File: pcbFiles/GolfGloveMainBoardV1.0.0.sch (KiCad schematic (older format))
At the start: 79 parts, among them J1 USB_C_Receptacle, J10 A-1JB, J11 Conn_01x16_Male, J12 HOST_WAKE, J13 TP4, J14 Conn_01x02_Male, J15 Conn_01x02_Male, J2 BT_UART, J3 USB_C_Receptacle, J4 Conn_01x01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

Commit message: Update the circuit schematic
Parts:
- removed C1, C10, C11, C12, C15, C16, C17, C18, C19, C2, C20, C27, C3, C34, C4, C5, C6, C7: C, Capacitors_SMD:C_0402, symbol C
- removed D1: LED, LEDs:LED_0603, symbol LED
- removed J14, J15, J6, J7, J8, J9: Conn_01x02_Male, Pin_Headers:Pin_Header_Straight_1x02_Pitch2.54mm, symbol Conn_01x02_Male
- removed L1: L, Inductors_SMD:L_0805, symbol L
- removed R1, R10, R12, R13, R14, R2, R3, R5, R6, R7, R8, R9: R, Capacitors_SMD:C_0603, symbol R
- removed SW2: SW_Push, Buttons_Switches_SMD:SW_SPST_B3S-1000, symbol SW_Push
- removed U1, U2: LSM9DS1TR, LSM9DS1TR:PQFN43P300X350X102-24N, symbol LSM9DS1TR
- removed U3: TPS63001DRCT, TPS63001DRCT:SON50P300X300X100-11N, symbol TPS63001DRCT
- removed U5: MCP73831T-2ACI/OT, MCP73831T-2ACI_OT:SOT95P280X145-5N, symbol MCP73831T-2ACI/OT
- removed U6: XC6119N16A7R-G, AAAA_XC6119_USPN-4:DFN-4, symbol XC6119N16A7R-G
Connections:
- wire segments 267 -> 192
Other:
- note removed: "0.033uf"
- note removed: "100nf"
- note removed: "10nf"
- note removed: "5.6k"
- moved on the sheet: C13, C14, C21, C22, C23, C24, C25, C26, C28, C29, C30, C31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

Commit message: updated uart comm lines
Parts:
- removed J2: BT_UART, Socket_Strips:Socket_Strip_Straight_1x04_Pitch2.54mm, symbol Conn_01x04_Female
- added J2: Conn_01x06, symbol Connector_Generic:Conn_01x06
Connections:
- net labels added: BT_UART_CTS, BT_UART_RTS, BT_UART_RX, BT_UART_TX
- wire segments 192 -> 237
- no-connect marks 0 -> 1
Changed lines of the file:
@@
-EESchema Schematic File Version 2
+EESchema Schematic File Version 4
 LIBS:power
-LIBS:device
-LIBS:switches
-LIBS:relays
-LIBS:motors
-LIBS:transistors
-LIBS:conn
-LIBS:linear
-LIBS:regul
 LIBS:74xx
-LIBS:cmos4000
-LIBS:adc-dac
-LIBS:memory
-LIBS:xilinx
-LIBS:microcontrollers
-LIBS:dsp
-LIBS:microchip
-LIBS:analog_switches
-LIBS:motorola
-LIBS:texas
-LIBS:intel
-LIBS:audio
-LIBS:interface
-LIBS:digital-audio
-LIBS:philips
-LIBS:display
-LIBS:cypress
-LIBS:siliconi
-LIBS:opto
-LIBS:atmel
-LIBS:contrib
-LIBS:valves
-LIBS:ADS1115IDGST
-LIBS:CYW20719B1KUMLG
-LIBS:LSM9DS1TR
-LIBS:TPS63001DRCT
-LIBS:MCP73831T-2ACI_OT
-LIBS:A-1JB
-LIBS:XC6119N16A7R-G
 LIBS:GolfGloveMainBoardV1.0.0-cache
-EELAYER 25 0
+EELAYER 26 0
 EELAYER END
 $Descr A4 11693 8268
@@
 	3900 2050 3825 2050
 Wire Wire Line
-	2925 3875 3400 3875
+	2925 3875 3025 3875
 Wire Wire Line
 	3325 3875 3325 3850
@@
 Connection ~ 3025 3875
 Wire Wire Line
-	1925 1825 2000 1825
-Wire Wire Line
-	1925 1925 2000 1925
+	1925 1825 1950 1825
+Wire Wire Line
+	1925 1925 1950 1925
 Wire Wire Line
 	1950 1925 1950 2025
@@
 Connection ~ 1950 1825
 Wire Wire Line
-	1950 825  1950 1225
+	1950 825  1950 925
 Wire Wire Line
 	1950 925  1925 925
@@
 Connection ~ 1950 1125
 Wire Wire Line
-	1025 3850 1475 3850
+	1025 3850 1125 3850
 Wire Wire Line
 	1425 3850 1425 3825
@@
 	7375 2375 7375 2425
 Wire Wire Line
-	7375 2425 7850 2425
-Wire Wire Line
-	7375 2725 7850 2725
+	7375 2425 7575 2425
+Wire Wire Line
+	7375 2725 7575 2725
 Connection ~ 7575 2725
 Connection ~ 7575 2425
@@
 GND
 Wire Wire Line
-	10300 1825 10300 2425
+	10300 1825 10300 1875
 Text GLabel 10575 3750 2    60   Input ~ 0
 Sensor3
@@
 Text GLabel 10575 3875 2    60   Input ~ 0
 Sensor4
-$Comp
-L Conn_01x04_Female J2
-U 1 1 5C4513F8
-P 7375 3825
-F 0 "J2" H 7275 4000 50  0000 C CNN
-F 1 "BT_UART" H 7525 3775 50  0000 C CNN
-F 2 "Socket_Strips:Socket_Strip_Straight_1x04_Pitch2.54mm" H 7375 3825 50  0001 C CNN
-F 3 "" H 7375 3825 50  0001 C CNN
-	1    7375 3825
-	-1   0    0    1
-$EndComp
-Wire Wire Line
-	7575 3625 7850 3625
-Wire Wire Line
-	7850 3725 7575 3725
-Wire Wire Line
-	7575 3825 7850 3825
-Wire Wire Line
-	7850 3925 7575 3925
+Wire Wire Line
+	7825 3625 7850 3625
+Wire Wire Line
+	7850 3725 7825 3725
+Wire Wire Line
+	7825 3825 7850 3825
+Wire Wire Line
+	7850 3925 7825 3925
 Text GLabel 9925 5125 2    60   Input ~ 0
 GND
@@
 SDA
 Wire Wire Line
-	9475 4325 9925 4325
-Wire Wire Line
-	9475 4625 9925 4625
+	9475 4325 9850 4325
+Wire Wire Line
+	9475 4625 9850 4625
 $Comp
 L EMI_Filter_LCL FL1
@@
 $EndComp
 Wire Wire Line
-	6775 4375 6775 4525
+	6775 4375 6775 4425
 Text GLabel 7075 4775 0    60   Input ~ 0
 GND
@@
 $EndComp
 Wire Wire Line
-	7375 4525 7475 4525
+	7375 4525 7400 4525
 Wire Wire Line
 	7775 4525 7850 4525
@@
 	7650 4775 7550 4775
 Wire Wire Line
-	7375 5275 7900 5275
+	7375 5275 7650 5275
 Wire Wire Line
 	7650 5275 7650 5175
@@
 	7225 3525 7175 3525
 Wire Wire Line
-	7150 3225 7850 3225
+	7150 3225 7225 3225
 Connection ~ 7225 3225
 Text Notes 6900 3400 0    60   ~ 0
@@
 $EndComp
 Wire Wire Line
-	10200 3100 10200 3175
+	10200 3100 10200 3125
 Wire Wire Line
 	10200 3100 7850 3100
@@
 Connection ~ 10200 3125
 Wire Wire Line
-	10200 3125 10450 3125
+	10200 3125 10375 3125
 Wire Wire Line
 	10375 3125 10375 3175
@@
 	10025 3025 9850 3025
 Wire Wire Line
-	10025 2875 10025 3025
+	10025 2875 10025 2950
 Text Notes 9925 3350 0    60   ~ 0
 1uf
@@
 	9900 2025 9900 1375
 Wire Wire Line
-	9450 1375 9950 1375
+	9450 1375 9550 1375
 $Comp
 L C C26
@@
 	9925 2125 9925 1575
 Wire Wire Line
-	9925 1575 10425 1575
-Wire Wire Line
-	10300 1875 10475 1875
+	9925 1575 10400 1575
+Wire Wire Line
+	10300 1875 10425 1875
 Connection ~ 10300 1875
 Wire Wire Line
@@
 	9950 2325 9950 1550
 Wire Wire Line
-	9950 1550 10625 1550
+	9950 1550 10400 1550
 Wire Wire Line
 	10625 1850 10475 1850
@@
 	10325 1375 10325 1325
 Wire Wire Line
-	10325 1325 10825 1325
+	10325 1325 10450 1325
 Connection ~ 10450 1325
 Wire Wire Line
-	9975 1525 10850 1525
+	9975 1525 10825 1525
 Wire Wire Line
 	9975 1525 9975 2225
@@
 24.000Mhz
 Wire Wire Line
-	9475 3425 10125 3425
+	9475 3425 9850 3425
 Wire Wire Line
 	10125 3425 10125 3775
@@
 	10100 3800 10100 3525
 Wire Wire Line
-	10100 3525 9475 3525
-Wire Wire Line
-	9475 4525 10400 4525
+	10100 3525 9850 3525
+Wire Wire Line
+	9475 4525 9850 4525
 Wire Wire Line
 	10400 4525 10400 3750
@@
 	10475 4125 10475 4925
 Wire Wire Line
-	10475 4925 9475 4925
+	10475 4925 9850 4925
 $Comp
 L Conn_01x16_Male J11
@@
 	9475 4025 9850 4025
 Wire Wire Line
-	9475 4125 9925 4125
-Wire Wire Line
-	9475 4225 10000 4225
+	9475 4125 9850 4125
+Wire Wire Line
+	9475 4225 9850 4225
 Connection ~ 9850 4325
 Wire Wire Line
@@
 Connection ~ 9850 4525
 Connection ~ 9850 4625
-Connection ~ 9850 4725
-Connection ~ 9850 4825
 Connection ~ 9850 4925
 Text GLabel 7775 2825 0    60   Input ~ 0
@@
 Wire Wire Line
 	5825 6900 5900 6900
+Wire Wire Line
+	3325 3875 3400 3875
+Wire Wire Line
+	3225 3875 3325 3875
+Wire Wire Line
+	3125 3875 3225 3875
+Wire Wire Line
+	3025 3875 3125 3875
+Wire Wire Line
+	1950 1925 2000 1925
+Wire Wire Line
+	1950 1825 2000 1825
+Wire Wire Line
+	1950 925  1950 1025
+Wire Wire Line
+	1950 1025 1950 1125
+Wire Wire Line
+	1950 1125 1950 1225
+Wire Wire Line
+	1425 3850 1475 3850
+Wire Wire Line
+	1325 3850 1425 3850
+Wire Wire Line
+	1225 3850 1325 3850
+Wire Wire Line
+	1125 3850 1225 3850
+Wire Wire Line
+	7575 2725 7850 2725
+Wire Wire Line
+	7575 2425 7850 2425
+Wire Wire Line
+	7650 5275 7900 5275
+Wire Wire Line
+	7225 3225 7850 3225
+Wire Wire Line
+	10200 3125 10200 3175
+Wire Wire Line
+	10375 3125 10450 3125
+Wire Wire Line
+	10025 2950 10025 3025
+Wire Wire Line
+	9550 1375 9900 1375
+Wire Wire Line
+	9900 1375 9950 1375
+Wire Wire Line
+	10300 1875 10300 2425
+Wire Wire Line
+	10425 1875 10475 1875
+Wire Wire Line
+	10400 1550 10450 1550
+Wire Wire Line
+	10400 1575 10425 1575
+Wire Wire Line
+	10450 1550 10625 1550
+Wire Wire Line
+	10450 1325 10825 1325
+Wire Wire Line
+	10825 1525 10850 1525
+Wire Wire Line
+	9850 3425 10125 3425
+Wire Wire Line
+	9850 3525 9475 3525
+Wire Wire Line
+	9850 4325 9925 4325
+Wire Wire Line
+	9850 4525 10400 4525
+Wire Wire Line
+	9850 4625 9925 4625
+Wire Wire Line
+	9850 4925 9475 4925
+Wire Wire Line
+	9850 4225 10000 4225
+Wire Wire Line
+	9850 4125 9925 4125
+Wire Wire Line
+	7400 4525 7475 4525
+Wire Wire Line
+	6775 4425 6775 4525
+$Comp
+L Connector_Generic:Conn_01x06 J2
+U 1 1 5C5A2335
+P 5550 3150
+F 0 "J2" H 5470 2625 50  0000 C CNN
+F 1 "Conn_01x06" H 5470 2716 50  0000 C CNN
+F 2 "" H 5550 3150 50  0001 C CNN
+F 3 "~" H 5550 3150 50  0001 C CNN
+	1    5550 3150
+	-1   0    0    1
+$EndComp
+Text Label 7825 3625 2    50   ~ 0
+BT_UART_RX
+Text Label 7825 3725 2    50   ~ 0
+BT_UART_TX
+Text Label 7825 3825 2    50   ~ 0
+BT_UART_RTS
+Text Label 7825 3925 2    50   ~ 0
+BT_UART_CTS
+Text GLabel 5800 3400 3    60   Input ~ 0
+GND
+Wire Wire Line
+	5750 3350 5800 3350
+Wire Wire Line
+	5800 3350 5800 3400
+Text Label 5800 3250 0    50   ~ 0
+BT_UART_RTS
+Text Label 5800 3050 0    50   ~ 0
+BT_UART_RX
+Text Label 5800 2950 0    50   ~ 0
+BT_UART_TX
+Text Label 5800 2850 0    50   ~ 0
+BT_UART_CTS
+Wire Wire Line
+	5750 2850 5800 2850
+Wire Wire Line
+	5750 2950 5800 2950
+Wire Wire Line
+	5750 3050 5800 3050
+Wire Wire Line
+	5750 3250 5800 3250
+NoConn ~ 5750 3150
 $EndSCHEMATC

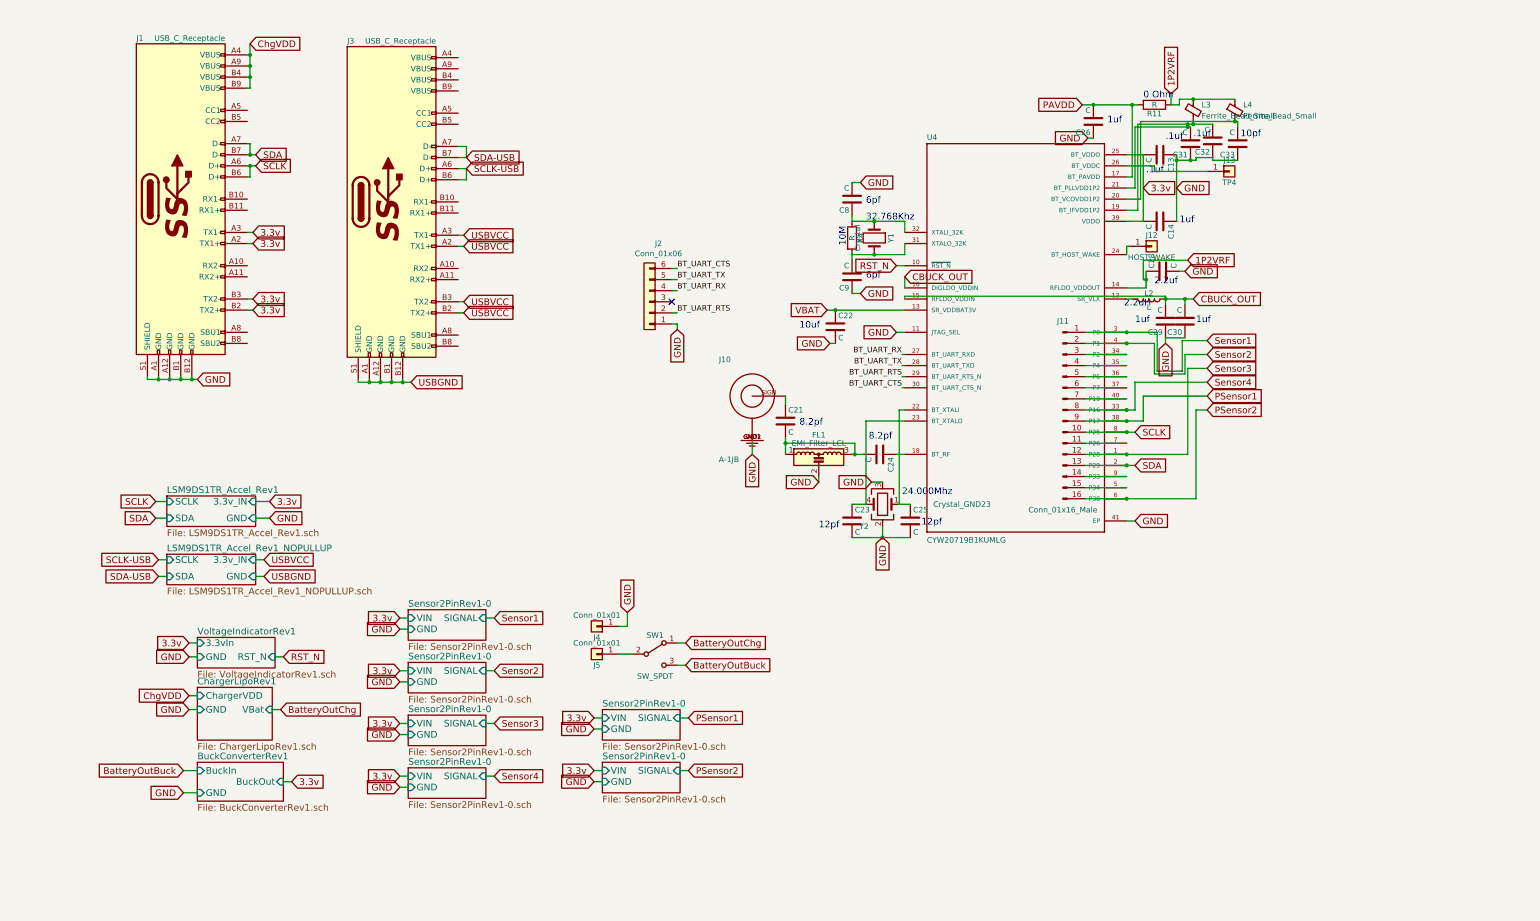
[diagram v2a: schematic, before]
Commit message: Update Footprints and Board Layers
Still need to get foorprint for x... device and the lpf may need to make them if I cannot find them @willcarroll7
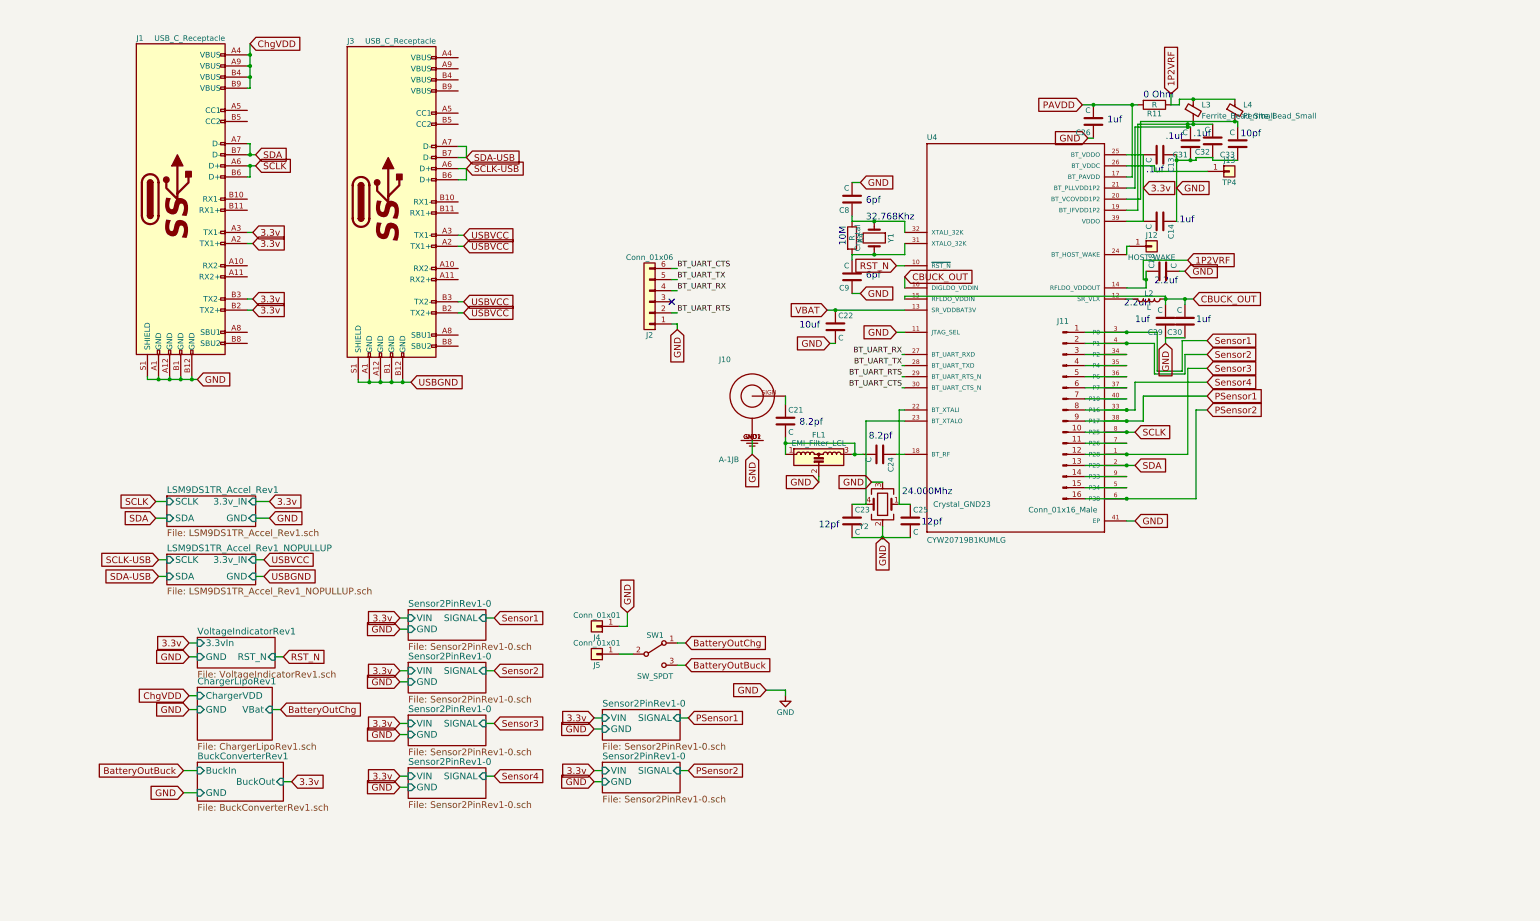
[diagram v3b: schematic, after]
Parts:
- removed J2: Conn_01x06, symbol Connector_Generic:Conn_01x06
- added J2: Conn_01x06, Pin_Headers:Pin_Header_Straight_1x06_Pitch2.54mm, symbol Conn_01x06
- R11, R4: footprint Capacitors_SMD:C_0603 -> Resistors_SMD:R_0402
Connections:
- net BT_UART_CTS: now also J2.6 (Pin_6)
- net BT_UART_RTS: now also J2.2 (Pin_2)
- net BT_UART_RX: now also J2.4 (Pin_4)
- net BT_UART_TX: now also J2.5 (Pin_5)
- net GND: now also J2.1 (Pin_1)
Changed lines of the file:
@@
-EESchema Schematic File Version 4
+EESchema Schematic File Version 2
 LIBS:power
+LIBS:device
+LIBS:switches
+LIBS:relays
+LIBS:motors
+LIBS:transistors
+LIBS:conn
+LIBS:linear
+LIBS:regul
 LIBS:74xx
+LIBS:cmos4000
+LIBS:adc-dac
+LIBS:memory
+LIBS:xilinx
+LIBS:microcontrollers
+LIBS:dsp
+LIBS:microchip
+LIBS:analog_switches
+LIBS:motorola
+LIBS:texas
+LIBS:intel
+LIBS:audio
+LIBS:interface
+LIBS:digital-audio
+LIBS:philips
+LIBS:display
+LIBS:cypress
+LIBS:siliconi
+LIBS:opto
+LIBS:atmel
+LIBS:contrib
+LIBS:valves
+LIBS:ADS1115IDGST
+LIBS:CYW20719B1KUMLG
+LIBS:LSM9DS1TR
+LIBS:TPS63001DRCT
+LIBS:MCP73831T-2ACI_OT
+LIBS:A-1JB
+LIBS:XC6119N16A7R-G
 LIBS:GolfGloveMainBoardV1.0.0-cache
-EELAYER 26 0
+EELAYER 25 0
 EELAYER END
 $Descr A4 11693 8268
@@
 F 0 "R4" V 7455 2575 50  0000 C CNN
 F 1 "R" V 7375 2575 50  0000 C CNN
-F 2 "Capacitors_SMD:C_0603" V 7305 2575 50  0001 C CNN
+F 2 "Resistors_SMD:R_0402" V 7305 2575 50  0001 C CNN
 F 3 "" H 7375 2575 50  0001 C CNN
 	1    7375 2575
@@
 	3900 2050 3825 2050
 Wire Wire Line
-	2925 3875 3025 3875
+	2925 3875 3400 3875
 Wire Wire Line
 	3325 3875 3325 3850
@@
 Connection ~ 3025 3875
 Wire Wire Line
-	1925 1825 1950 1825
-Wire Wire Line
-	1925 1925 1950 1925
+	1925 1825 2000 1825
+Wire Wire Line
+	1925 1925 2000 1925
 Wire Wire Line
 	1950 1925 1950 2025
@@
 Connection ~ 1950 1825
 Wire Wire Line
-	1950 825  1950 925
+	1950 825  1950 1225
 Wire Wire Line
 	1950 925  1925 925
@@
 Connection ~ 1950 1125
 Wire Wire Line
-	1025 3850 1125 3850
+	1025 3850 1475 3850
 Wire Wire Line
 	1425 3850 1425 3825
@@
 	7375 2375 7375 2425
 Wire Wire Line
-	7375 2425 7575 2425
-Wire Wire Line
-	7375 2725 7575 2725
+	7375 2425 7850 2425
+Wire Wire Line
+	7375 2725 7850 2725
 Connection ~ 7575 2725
 Connection ~ 7575 2425
@@
 GND
 Wire Wire Line
-	10300 1825 10300 1875
+	10300 1825 10300 2425
 Text GLabel 10575 3750 2    60   Input ~ 0
 Sensor3
@@
 SDA
 Wire Wire Line
-	9475 4325 9850 4325
-Wire Wire Line
-	9475 4625 9850 4625
+	9475 4325 9925 4325
+Wire Wire Line
+	9475 4625 9925 4625
 $Comp
 L EMI_Filter_LCL FL1
@@
 $EndComp
 Wire Wire Line
-	6775 4375 6775 4425
+	6775 4375 6775 4525
 Text GLabel 7075 4775 0    60   Input ~ 0
 GND
@@
 $EndComp
 Wire Wire Line
-	7375 4525 7400 4525
+	7375 4525 7475 4525
 Wire Wire Line
 	7775 4525 7850 4525
@@
 	7650 4775 7550 4775
 Wire Wire Line
-	7375 5275 7650 5275
+	7375 5275 7900 5275
 Wire Wire Line
 	7650 5275 7650 5175
@@
 	7225 3525 7175 3525
 Wire Wire Line
-	7150 3225 7225 3225
+	7150 3225 7850 3225
 Connection ~ 7225 3225
 Text Notes 6900 3400 0    60   ~ 0
@@
 $EndComp
 Wire Wire Line
-	10200 3100 10200 3125
+	10200 3100 10200 3175
 Wire Wire Line
 	10200 3100 7850 3100
@@
 Connection ~ 10200 3125
 Wire Wire Line
-	10200 3125 10375 3125
+	10200 3125 10450 3125
 Wire Wire Line
 	10375 3125 10375 3175
@@
 	10025 3025 9850 3025
 Wire Wire Line
-	10025 2875 10025 2950
+	10025 2875 10025 3025
 Text Notes 9925 3350 0    60   ~ 0
 1uf
@@
 	9900 2025 9900 1375
 Wire Wire Line
-	9450 1375 9550 1375
+	9450 1375 9950 1375
 $Comp
 L C C26
@@
 F 0 "R11" V 10180 1375 50  0000 C CNN
 F 1 "R" V 10100 1375 50  0000 C CNN
-F 2 "Capacitors_SMD:C_0603" V 10030 1375 50  0001 C CNN
+F 2 "Resistors_SMD:R_0402" V 10030 1375 50  0001 C CNN
 F 3 "" H 10100 1375 50  0001 C CNN
 	1    10100 1375
@@
 	9925 2125 9925 1575
 Wire Wire Line
-	9925 1575 10400 1575
-Wire Wire Line
-	10300 1875 10425 1875
+	9925 1575 10425 1575
+Wire Wire Line
+	10300 1875 10475 1875
 Connection ~ 10300 1875
 Wire Wire Line
@@
 	9950 2325 9950 1550
 Wire Wire Line
-	9950 1550 10400 1550
+	9950 1550 10625 1550
 Wire Wire Line
 	10625 1850 10475 1850
@@
 Connection ~ 10425 1875
 Wire Wire Line
-	10400 1575 10400 1550
+	10400 1550 10400 1575
 Connection ~ 10400 1550
 Connection ~ 10400 1575
@@
 	10325 1375 10325 1325
 Wire Wire Line
-	10325 1325 10450 1325
+	10325 1325 10825 1325
 Connection ~ 10450 1325
 Wire Wire Line
-	9975 1525 10825 1525
+	9975 1525 10850 1525
 Wire Wire Line
 	9975 1525 9975 2225
@@
 24.000Mhz
 Wire Wire Line
-	9475 3425 9850 3425
+	9475 3425 10125 3425
 Wire Wire Line
 	10125 3425 10125 3775
@@
 	10100 3800 10100 3525
 Wire Wire Line
-	10100 3525 9850 3525
-Wire Wire Line
-	9475 4525 9850 4525
+	10100 3525 9475 3525
+Wire Wire Line
+	9475 4525 10400 4525
 Wire Wire Line
 	10400 4525 10400 3750
@@
 	10475 4125 10475 4925
 Wire Wire Line
-	10475 4925 9850 4925
+	10475 4925 9475 4925
 $Comp
 L Conn_01x16_Male J11
@@
 	9475 4025 9850 4025
 Wire Wire Line
-	9475 4125 9850 4125
-Wire Wire Line
-	9475 4225 9850 4225
+	9475 4125 9925 4125
+Wire Wire Line
+	9475 4225 10000 4225
 Connection ~ 9850 4325
 Wire Wire Line
@@
 Wire Wire Line
 	5825 6900 5900 6900
-Wire Wire Line
-	3325 3875 3400 3875
-Wire Wire Line
-	3225 3875 3325 3875
-Wire Wire Line
-	3125 3875 3225 3875
-Wire Wire Line
-	3025 3875 3125 3875
-Wire Wire Line
-	1950 1925 2000 1925
-Wire Wire Line
-	1950 1825 2000 1825
-Wire Wire Line
-	1950 925  1950 1025
-Wire Wire Line
-	1950 1025 1950 1125
-Wire Wire Line
-	1950 1125 1950 1225
-Wire Wire Line
-	1425 3850 1475 3850
-Wire Wire Line
-	1325 3850 1425 3850
-Wire Wire Line
-	1225 3850 1325 3850
-Wire Wire Line
-	1125 3850 1225 3850
-Wire Wire Line
-	7575 2725 7850 2725
-Wire Wire Line
-	7575 2425 7850 2425
-Wire Wire Line
-	7650 5275 7900 5275
-Wire Wire Line
-	7225 3225 7850 3225
-Wire Wire Line
-	10200 3125 10200 3175
-Wire Wire Line
-	10375 3125 10450 3125
-Wire Wire Line
-	10025 2950 10025 3025
-Wire Wire Line
-	9550 1375 9900 1375
-Wire Wire Line
-	9900 1375 9950 1375
-Wire Wire Line
-	10300 1875 10300 2425
-Wire Wire Line
-	10425 1875 10475 1875
-Wire Wire Line
-	10400 1550 10450 1550
-Wire Wire Line
-	10400 1575 10425 1575
-Wire Wire Line
-	10450 1550 10625 1550
-Wire Wire Line
-	10450 1325 10825 1325
-Wire Wire Line
-	10825 1525 10850 1525
-Wire Wire Line
-	9850 3425 10125 3425
-Wire Wire Line
-	9850 3525 9475 3525
-Wire Wire Line
-	9850 4325 9925 4325
-Wire Wire Line
-	9850 4525 10400 4525
-Wire Wire Line
-	9850 4625 9925 4625
-Wire Wire Line
-	9850 4925 9475 4925
-Wire Wire Line
-	9850 4225 10000 4225
-Wire Wire Line
-	9850 4125 9925 4125
-Wire Wire Line
-	7400 4525 7475 4525
-Wire Wire Line
-	6775 4425 6775 4525
-$Comp
-L Connector_Generic:Conn_01x06 J2
-U 1 1 5C5A2335
-P 5550 3150
-F 0 "J2" H 5470 2625 50  0000 C CNN
-F 1 "Conn_01x06" H 5470 2716 50  0000 C CNN
-F 2 "" H 5550 3150 50  0001 C CNN
-F 3 "~" H 5550 3150 50  0001 C CNN
-	1    5550 3150
-	-1   0    0    1
-$EndComp
 Text Label 7825 3625 2    50   ~ 0
 BT_UART_RX
@@
 	5750 3250 5800 3250
 NoConn ~ 5750 3150
+$Comp
+L Conn_01x06 J2
+U 1 1 5C598653
+P 5550 3150
+F 0 "J2" H 5550 3450 50  0000 C CNN
+F 1 "Conn_01x06" H 5550 2750 50  0000 C CNN
+F 2 "Pin_Headers:Pin_Header_Straight_1x06_Pitch2.54mm" H 5550 3150 50  0001 C CNN
+F 3 "" H 5550 3150 50  0001 C CNN
+	1    5550 3150
+	-1   0    0    1
+$EndComp
+Text GLabel 6600 6650 0    60   Input ~ 0
+GND
+$Comp
+L GND #PWR?
+U 1 1 5C59B296
+P 6775 6700
+F 0 "#PWR?" H 6775 6450 50  0001 C CNN
+F 1 "GND" H 6775 6550 50  0000 C CNN
+F 2 "" H 6775 6700 50  0001 C CNN
+F 3 "" H 6775 6700 50  0001 C CNN
+	1    6775 6700
+	1    0    0    -1
+$EndComp
+Wire Wire Line
+	6600 6650 6775 6650
+Wire Wire Line
+	6775 6650 6775 6700
 $EndSCHEMATC
